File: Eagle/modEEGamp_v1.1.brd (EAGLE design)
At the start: 111.1 x 57.1 mm, 118 parts, among them IC2 INA217DW, IC204 TLC277P, IC3 INA217DW, P1 20k, P203 20k, Q1 BC547, Q2 BC557, Q202 BC557, Q204 BC557, Q206 BC547, Q208 BC547, Q3 BC547, Q4 BC557

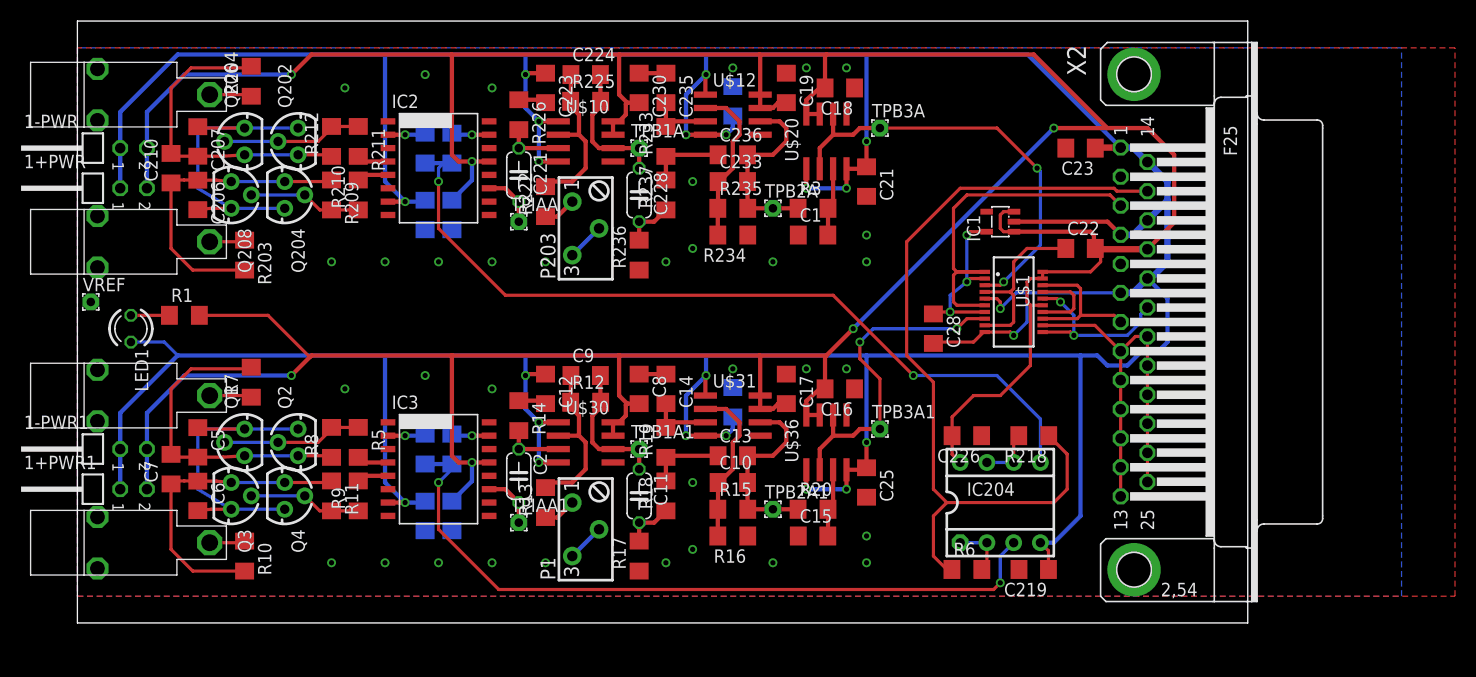
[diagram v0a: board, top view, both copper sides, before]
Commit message: Added mounting holes
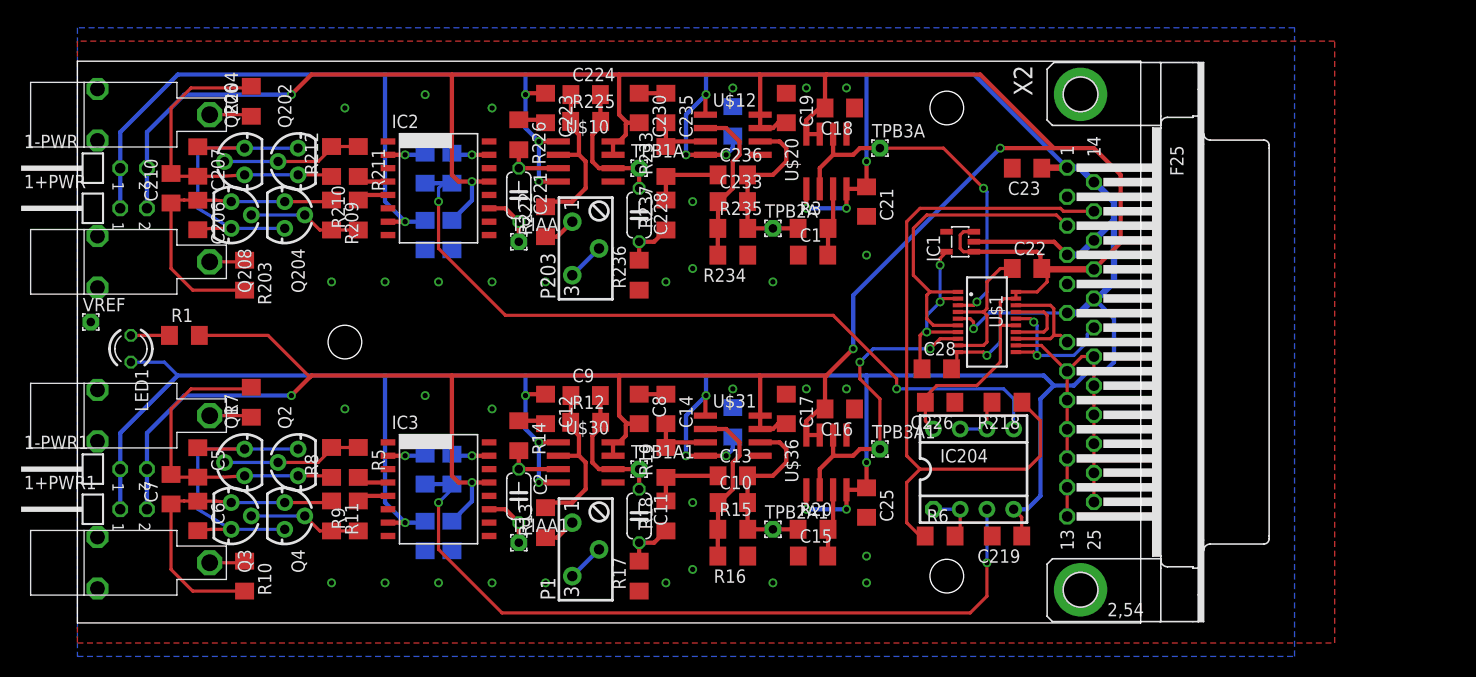
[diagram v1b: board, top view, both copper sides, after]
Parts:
- moved C22 5.43 mm to (90.2, 33.7)
- moved C23 5.43 mm to (90.2, 43.2)
- moved X2 5.43 mm to (95.2, 26.7)
- moved IC1 4.26 mm to (83.8, 36.2)
- moved C219 4.07 mm to (88.3, 8.26)
- moved R218 4.07 mm to (88.3, 21.0)
- moved IC204 4.07 mm to (85.1, 14.6)
- moved R6 4.07 mm to (81.9, 8.26)
- moved C226 4.07 mm to (81.9, 21.0)
- moved C28 3.82 mm to (81.6, 24.1), turned to 0 degrees
- moved U$1 3.18 mm to (86.4, 28.6)
- moved 1+PWR 1.91 mm to (2.54, 39.4)
- moved 1-PWR 1.91 mm to (2.54, 43.2)
- moved 1-PWR1 1.91 mm to (2.54, 14.6)
- moved C1 1.91 mm to (69.8, 34.9)
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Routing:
- net AGND: track 460.2 -> 436.9 mm
- net +5V/2: track 380.8 -> 365.5 mm
- net N$66: track 77.1 -> 68.1 mm
- net ADIN0: track 41.2 -> 35.1 mm
- net N$12: track 78.5 -> 73.7 mm
- net N$1: track 34.4 -> 30.8 mm
- net N$16: track 69.6 -> 72.7 mm
- net CNV: track 17.1 -> 14.2 mm
- net VCOM: track 97.9 -> 95.4 mm, vias 34 -> 33
- net ADIN1: track 32.3 -> 29.7 mm
- net SCK: track 14.5 -> 12.0 mm
- net N$3: track 39.2 -> 36.6 mm
- net N$2: track 16.8 -> 17.5 mm
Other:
- board size 111.1 x 57.1 mm -> 101 x 53.3 mm

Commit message: Board updates (jumpers)
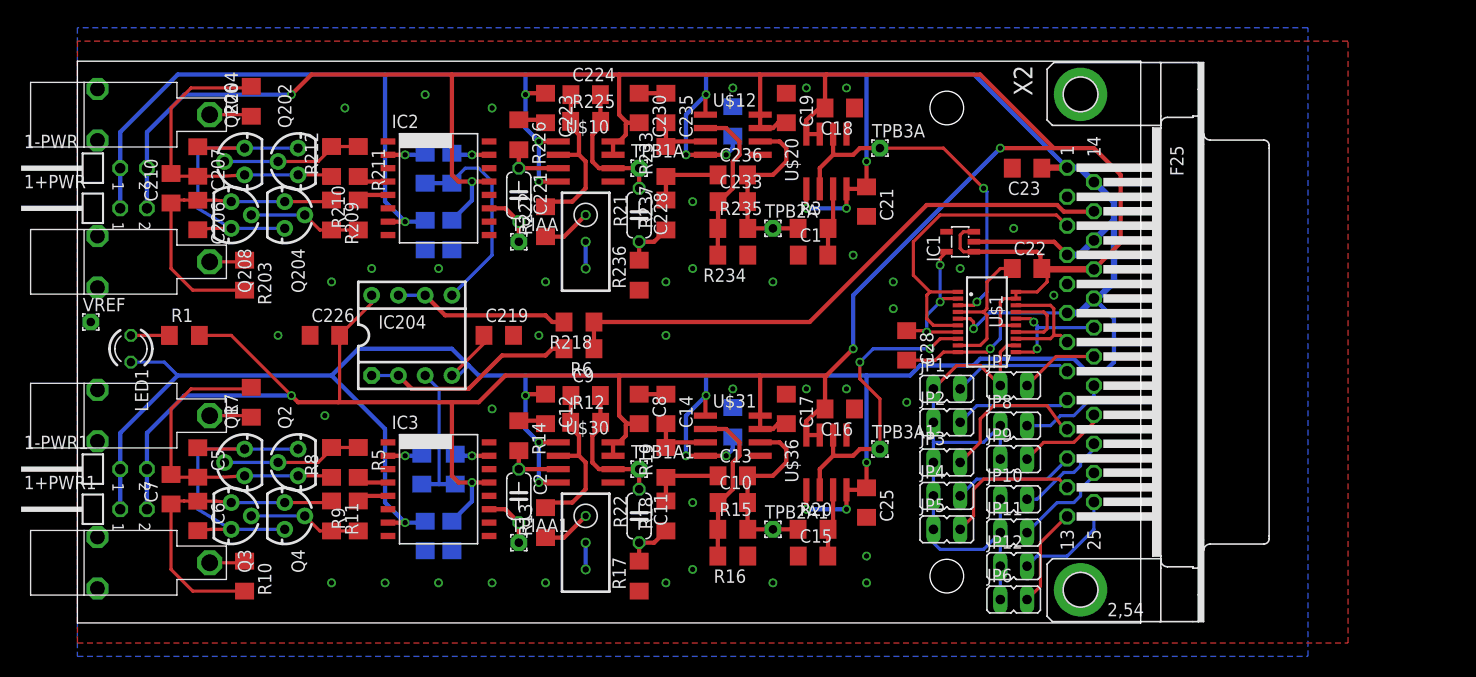
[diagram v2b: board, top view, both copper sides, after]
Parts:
- removed P1, P203: 20k, TRIMPOT@2:S64Y
- added JP1, JP10, JP11, JP12, JP2, JP3, JP4, JP5, JP6, JP7, JP8, JP9: (no value), jumper:JP1
- added R21, R22: 20k, resistor:RTRIM3296W
- IC1: value (none) -> 2.5V
- moved C226 58.8 mm to (23.5, 27.3), turned to 0 degrees
- moved IC204 54.8 mm to (31.8, 27.3)
- moved C219 51.9 mm to (40.0, 27.3), turned to 0 degrees
- moved R218 41.3 mm to (47.6, 28.6)
- moved R6 38.6 mm to (47.6, 26.0), turned to 180 degrees
- moved C28 3.62 mm to (78.7, 26.4), turned to 270 degrees
- moved R2 0.32 mm to (32.7, 14.6)
- moved R4 0.32 mm to (35.9, 14.6)
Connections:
- new net N$10: JP1.2, X2.8
- new net N$11: JP2.2, X2.9
- new net N$55: JP5.2, X2.12
- new net N$56: JP6.2, X2.13
- new net N$58: JP7.2, X2.20
- new net N$59: JP8.2, X2.21
- new net N$6: R13.1, R22.1
- new net N$60: JP9.2, X2.22
- new net N$61: JP10.2, X2.23
- new net N$62: JP11.2, X2.24
- new net N$63: JP12.2, X2.25
- new net N$8: R21.1, R222.1
- net N$3: now also JP1.1, JP10.1, JP11.1, JP12.1, JP2.1, JP3.1, JP4.1, JP5.1, JP6.1, JP7.1, JP8.1, JP9.1; no longer X2.10, X2.11, X2.12, X2.13, X2.20, X2.21, X2.22, X2.23, X2.24, X2.25, X2.8, X2.9
- net N$36: now also JP3.2, X2.10; no longer P1.1, R13.1
- net N$40: now also JP4.2, X2.11; no longer P203.1, R222.1
- net VCOM: now also R21.2, R21.3, R22.2, R22.3; no longer P1.2, P1.3, P203.2, P203.3
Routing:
- net N$16: track 72.7 -> 14.0 mm, vias 2 -> 0
- net N$12: track 73.7 -> 19.9 mm, vias 2 -> 0
- net N$3: track 36.6 -> 54.6 mm
- net N$35: track 5.28 -> 20.4 mm
- net N$55: track 0.00 -> 13.9 mm
- net N$66: track 68.1 -> 54.9 mm
- net N$36: track 3.13 -> 14.9 mm
- net N$52: track 5.28 -> 16.8 mm
- net N$10: track 0.00 -> 11.3 mm
- net N$11: track 0.00 -> 11.0 mm
- net N$63: track 0.00 -> 10.4 mm
- net N$56: track 0.00 -> 9.49 mm
- net N$62: track 0.00 -> 9.24 mm
- net N$61: track 0.00 -> 9.02 mm
- net N$40: track 3.13 -> 11.7 mm
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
